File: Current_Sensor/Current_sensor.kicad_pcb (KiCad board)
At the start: 2 copper layers, 102.9 x 66 mm, 38 parts, among them P1 CONN_01X04, P2 CONN_01X02, P3 CONN_01X03, U1 LTS-25-NP, U2 LTS-25-NP, U3 LTS-25-NP, U4 NE5532, U5 NE5532, U6 NE5532

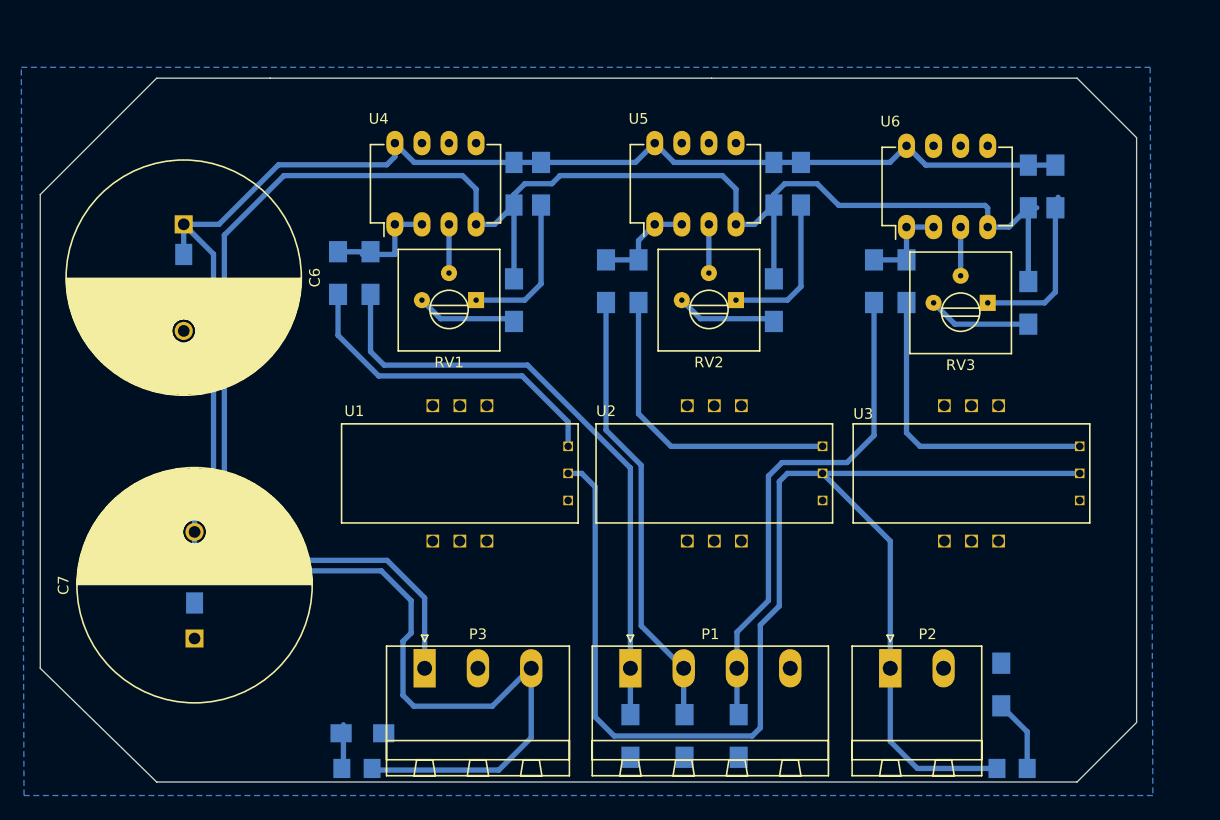
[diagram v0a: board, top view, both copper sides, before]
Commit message: Updated current sensor card
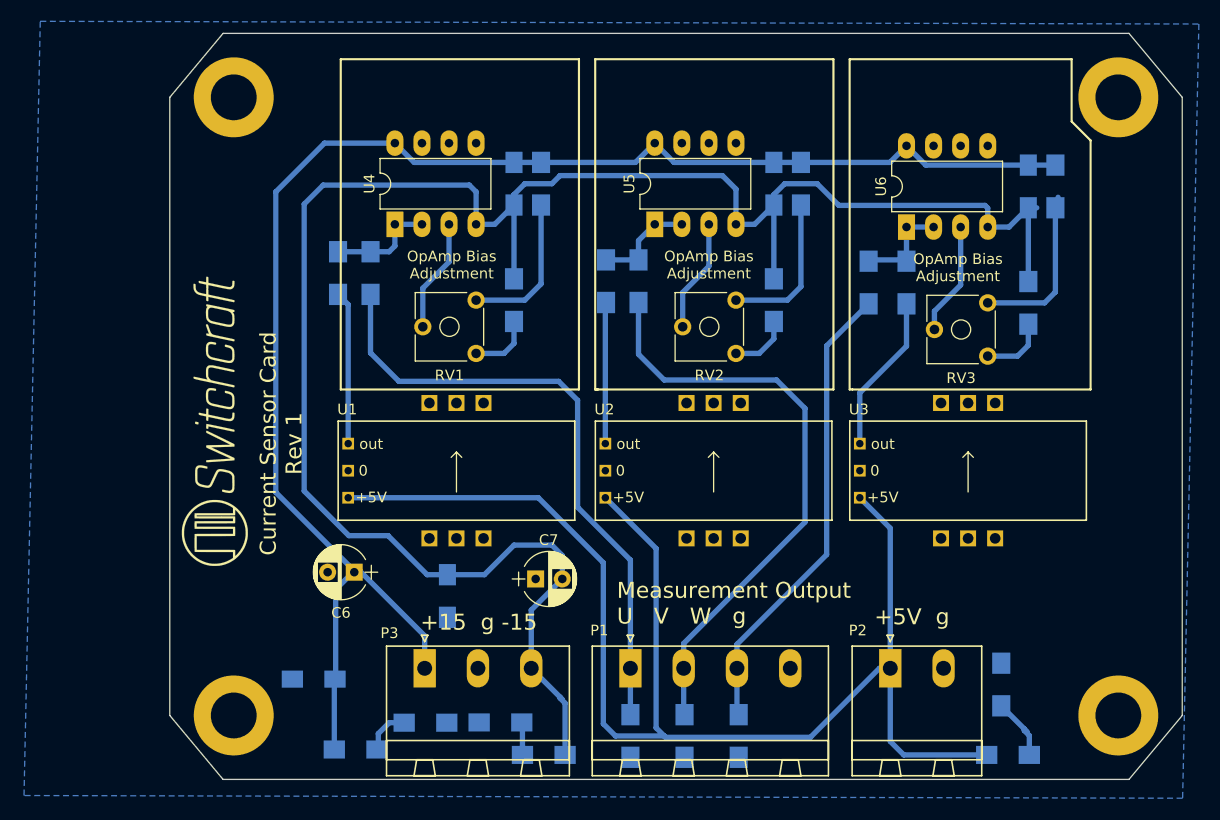
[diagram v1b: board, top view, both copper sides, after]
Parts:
- added D3: LED, LEDs:LED_1206_HandSoldering, B.Cu at (85.1, 155.7)
- added G***: LOGO, Switchcraft:Switchcraft_medium_logo, F.Cu at (54.2, 124.2)
- added R18: R, Resistors_SMD:R_1206_HandSoldering, B.Cu at (81.0, 152.7)
- added REF**: MountingHole_4.3mm_M4_DIN965_Pad, Mounting_Holes:MountingHole_4.3mm_M4_DIN965_Pad, F.Cu at (56.0, 94.0)
- added REF**: MountingHole_4.3mm_M4_DIN965_Pad, Mounting_Holes:MountingHole_4.3mm_M4_DIN965_Pad, F.Cu at (139.0, 94.0)
- added REF**: MountingHole_4.3mm_M4_DIN965_Pad, Mounting_Holes:MountingHole_4.3mm_M4_DIN965_Pad, F.Cu at (56.0, 152.0)
- added REF**: MountingHole_4.3mm_M4_DIN965_Pad, Mounting_Holes:MountingHole_4.3mm_M4_DIN965_Pad, F.Cu at (139.0, 152.0)
- C6, C7: footprint Capacitors_ThroughHole:C_Radial_D22_L41_P10 -> Capacitors_THT:CP_Radial_D5.0mm_P2.50mm
- D1, D2: footprint LEDs:LED_1206 -> LEDs:LED_1206_HandSoldering
- RV1, RV2, RV3: footprint potentiometer:Potentiometer_Trimmer-Suntan-TSR-3386P -> Potentiometers:Potentiometer_Trimmer_ACP_CA6v_Horizontal
- moved C4 39.8 mm to (63.5, 148.6), turned to 180 degrees
- moved C6 36.4 mm to (67.3, 138.6), turned to 180 degrees
- moved C7 32.5 mm to (84.3, 139.2), turned to 0 degrees
- moved C5 23.8 mm to (76.0, 140.8)
- moved R16 6.00 mm to (74.0, 152.7)
- moved U1 4.33 mm to (72.9, 129.0)
- moved U3 4.33 mm to (120.9, 129.0)
- moved U2 4.07 mm to (97.0, 129.0)
- moved R11 3.05 mm to (94.0, 111.3)
- moved R2 3.05 mm to (90.9, 111.3)
- moved D1 1.78 mm to (67.4, 155.2), turned to 180 degrees
- moved D2 1.33 mm to (128.7, 155.7)
- moved R12 0.52 mm to (115.6, 111.4)
- moved R3 0.13 mm to (119.1, 111.4)
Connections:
- P3 pad 1: -15V -> +15V
- P3 pad 3: +15V -> -15V
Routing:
- net +15V: track 199.6 -> 147.6 mm
- net Net-(R1-Pad2): track 30.8 -> 14.4 mm
- net Net-(R2-Pad2): track 29.0 -> 13.3 mm
- net Net-(P1-Pad2): track 42.2 -> 56.5 mm
- net Net-(R3-Pad2): track 29.0 -> 14.9 mm
- net -15V: track 177.3 -> 183.9 mm
- net Net-(RV3-Pad2): track 4.57 -> 10.6 mm
- net Net-(RV2-Pad2): track 4.57 -> 10.6 mm
- net Net-(RV1-Pad2): track 4.57 -> 10.6 mm
- net Net-(R7-Pad1): track 9.40 -> 5.75 mm
- net Net-(R9-Pad1): track 9.72 -> 6.22 mm
- net Net-(P1-Pad3): track 47.8 -> 44.3 mm
- net Net-(R5-Pad1): track 9.36 -> 6.01 mm
- net Net-(D3-Pad2): track 0.00 -> 3.07 mm
- net +5V: track 132.4 -> 130.0 mm
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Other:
- board size 102.9 x 66 mm -> 95 x 70 mm
- board text added: "+15 g -15"
- board text added: "+15V OK"
- board text added: "+5V OK"
- board text added: "+5V g"
- board text added: "-15V OK"
- board text added: "Current Sensor Card Rev 1"
- board text added: "Measurement Output U V W g"
- board text added: "OpAmp Bias Adjustment"
- board text added: "Yngve was here"

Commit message: Finalized - Ready for production
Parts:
- added REF***: OSHW-Logo2_7.3x6mm_SilkScreen, OSHW:OSHW-Logo2_7.3x6mm_SilkScreen, F.Cu at (54.4, 103.6)
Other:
- board text added: "Not that anyone cares what I say, but the restaurant is at the *other* end of the Universe."

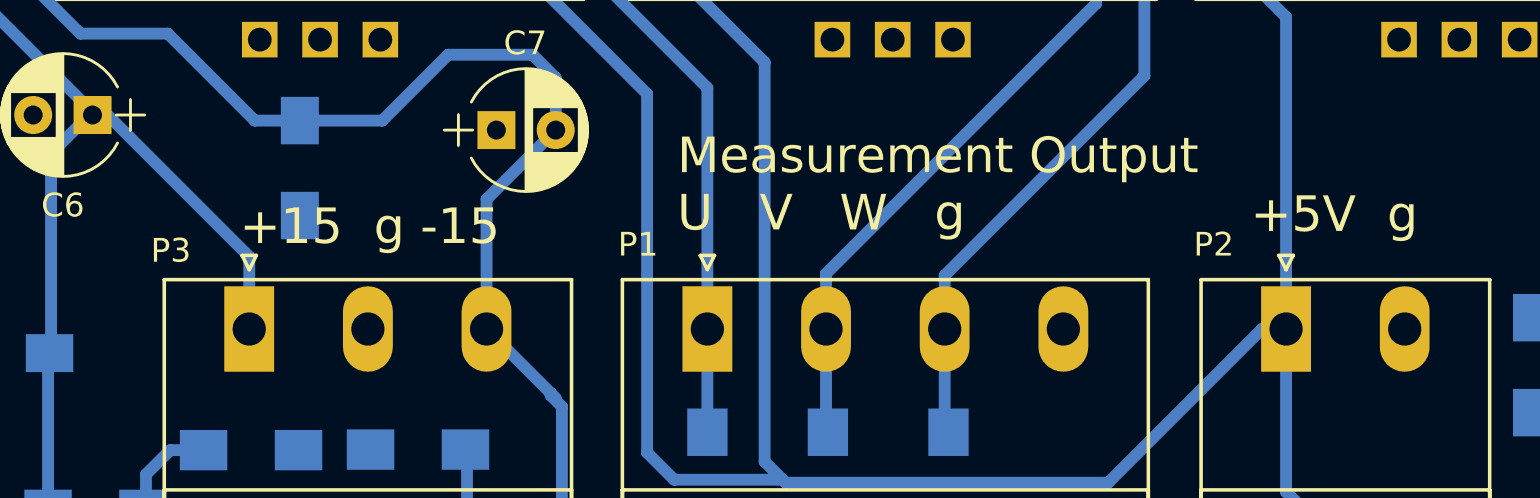
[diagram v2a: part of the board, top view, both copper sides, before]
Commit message: Corrected library reference to phoenix connectors
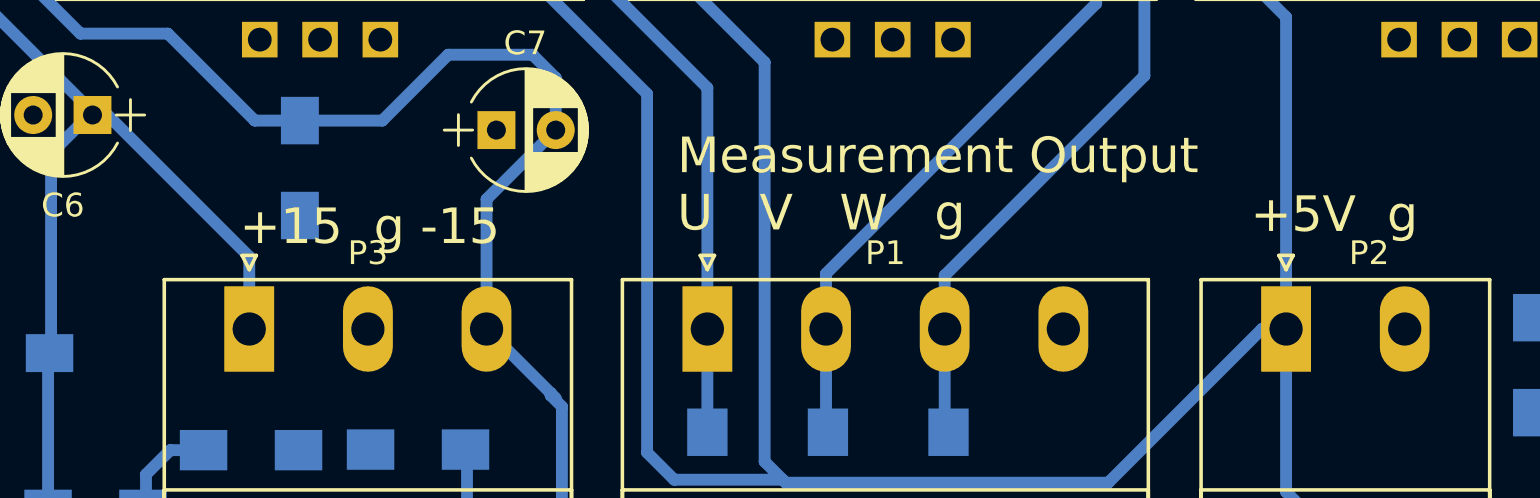
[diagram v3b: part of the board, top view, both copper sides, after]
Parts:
- P1: footprint phoenix:PhoenixContact_MSTBA-G_04x5.00mm_Angled -> PhoenixContact:MSTBA_25_4p_G_508-1757268
- P2: footprint phoenix:PhoenixContact_MSTBA-G_02x5.00mm_Angled -> PhoenixContact:MSTBA_25_2p_G_508-1757242
- P3: footprint phoenix:PhoenixContact_MSTBA-G_03x5.00mm_Angled -> PhoenixContact:MSTBA_25_3p_G_508-1757488

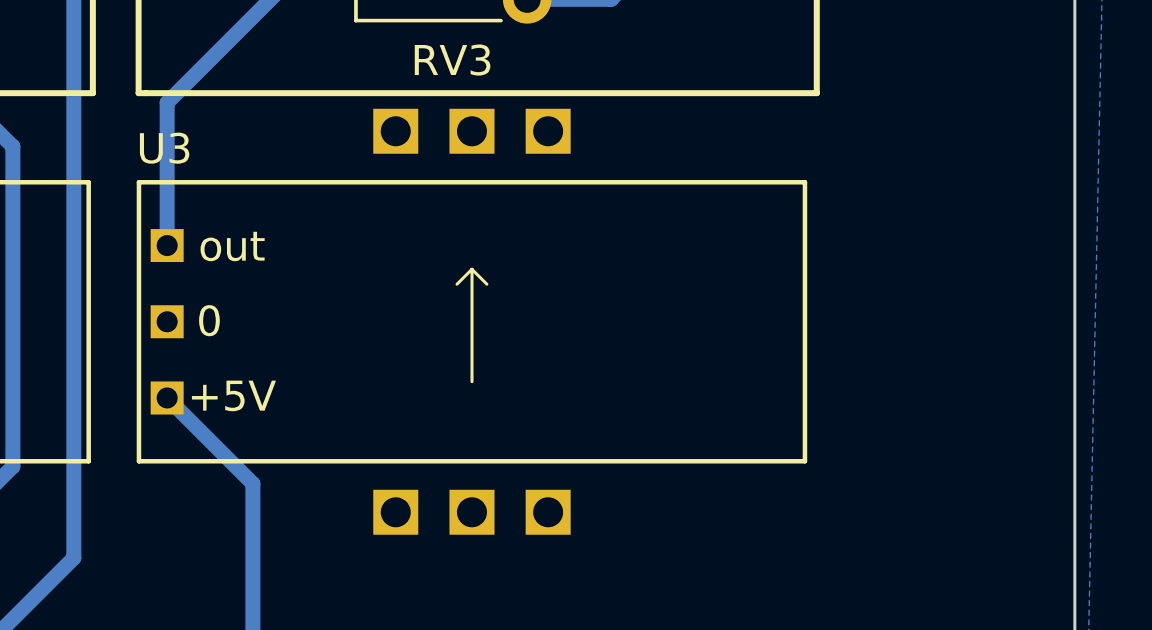
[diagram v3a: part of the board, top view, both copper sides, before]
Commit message: Updated component values and highlighted errors and/or improvement possibilities for next revision
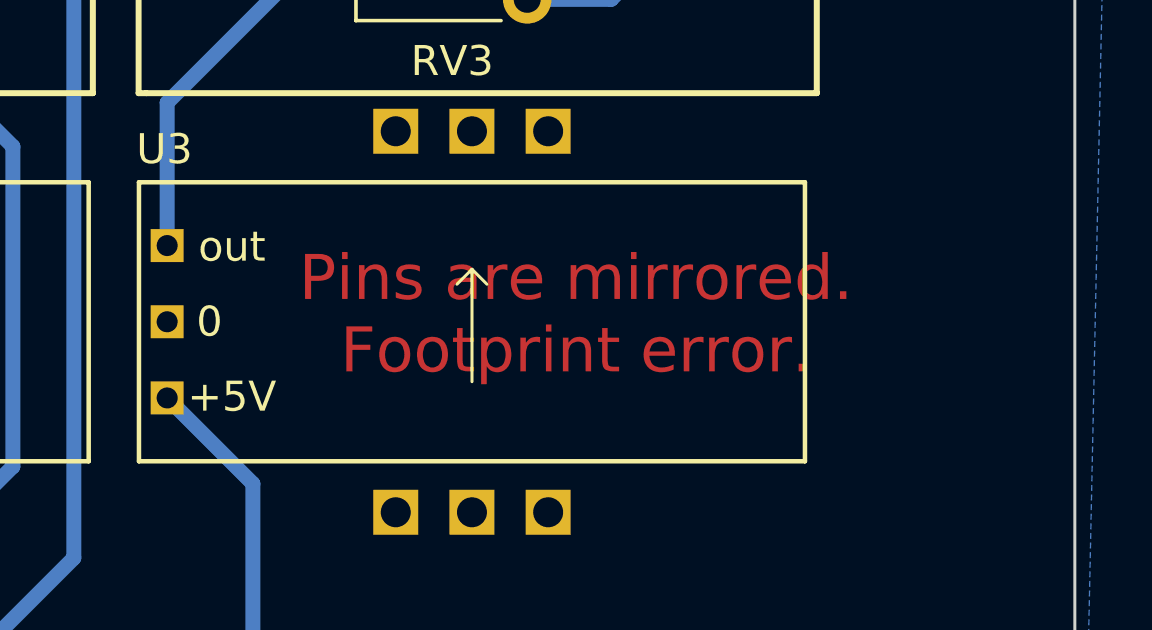
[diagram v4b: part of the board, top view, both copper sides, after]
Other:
- board text added: "Pins are mirrored. Footprint error."
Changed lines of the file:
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@@
     (links 73)
     (no_connects 0)
-    (area 49.949999 87.949999 145.050001 158.050001)
+    (area 36.322 81.372723 156.186 160.149)
     (thickness 1.6)
-    (drawings 39)
+    (drawings 40)
     (tracks 173)
     (zones 0)
@@
     )
   )
+  (gr_text "Pins are mirrored. \nFootprint error." (at 128.372 128.784) (layer F.Cu)
+    (effects (font (size 1.5 1.5) (thickness 0.3)))
+  )
   (gr_text "Not that anyone cares what I say, but the restaurant is at the *other* end of the Universe. " (at 100.584 92.71) (layer B.SilkS)
